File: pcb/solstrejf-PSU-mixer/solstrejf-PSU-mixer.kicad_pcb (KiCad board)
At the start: 2 copper layers, 36 parts, among them J1 LEFT_JACK, J2 RIGHT_JACK, J3 Conn_02x05_Odd_Even, J4 Conn_02x05_Odd_Even, J5 Conn_02x05_Odd_Even, J6 Conn_02x05_Odd_Even, J7 Transformer_Terminals, U1 Opamp_Dual, U2 L7815, U3 L7915

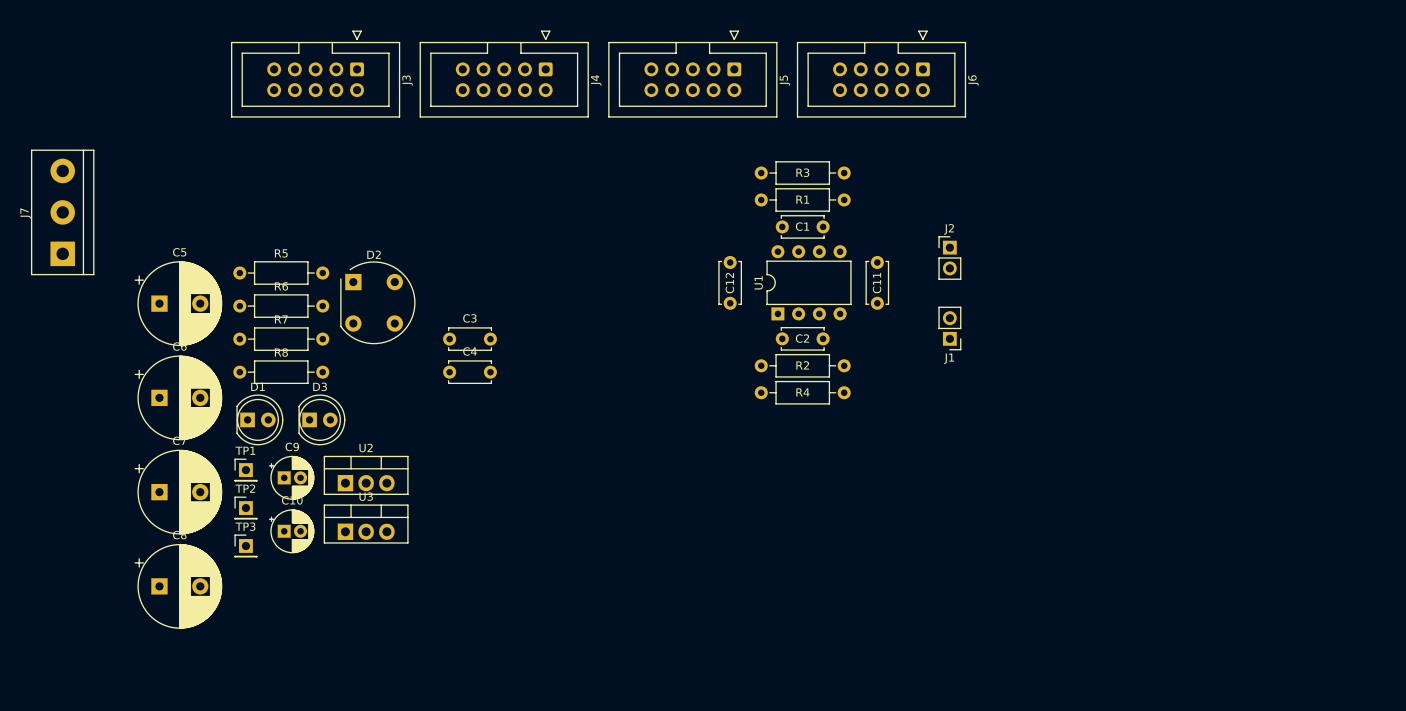
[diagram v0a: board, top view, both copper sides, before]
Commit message: updated KiCad schematic and PCB with the new changes added to the TIA after LTspice simulations.
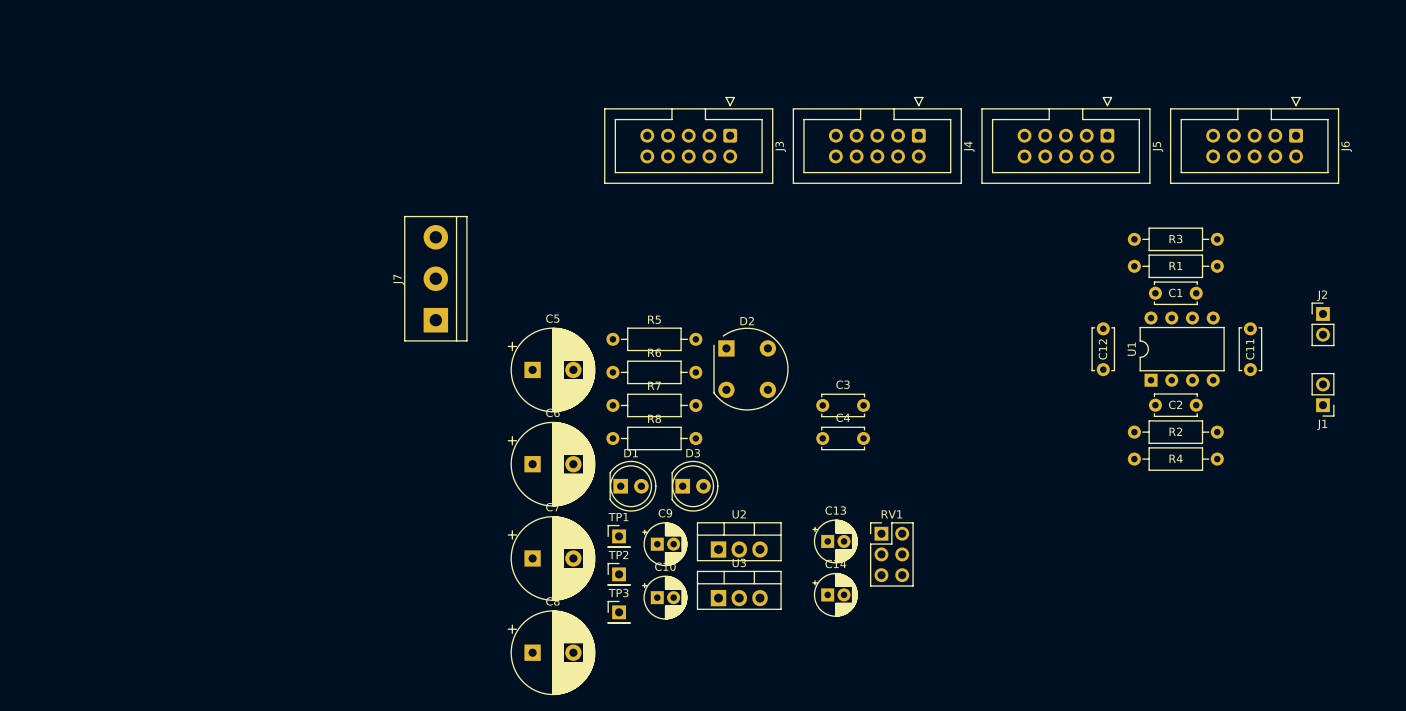
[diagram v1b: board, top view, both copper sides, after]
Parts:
- added C13: 1uF, Capacitor_THT:CP_Radial_D5.0mm_P2.00mm, F.Cu at (115.3, 114.5)
- added C14: 1uF, Capacitor_THT:CP_Radial_D5.0mm_P2.00mm, F.Cu at (115.3, 121.0)
- added RV1: 100k-A, Connector_PinHeader_2.54mm:PinHeader_2x03_P2.54mm_Vertical, F.Cu at (121.9, 113.5)
- C1, C2: value 2n2 -> 1nF
- R1, R2: value 5k -> 10k
- moved C12 46.4 mm to (149.1, 93.4)
- moved R1 46.4 mm to (163.1, 80.8)
- moved R2 46.4 mm to (163.1, 101.1)
- moved C10 46.4 mm to (94.5, 121.4)
- moved C5 46.4 mm to (79.2, 93.5)
- moved C6 46.4 mm to (79.2, 105.0)
- moved C7 46.4 mm to (79.2, 116.6)
- moved C8 46.4 mm to (79.2, 128.1)
- moved C9 46.4 mm to (94.5, 114.8)
- moved D2 46.4 mm to (102.9, 90.8)
- moved D3 46.4 mm to (97.6, 107.7)
- moved R5 46.4 mm to (89.0, 89.7)
- moved R6 46.4 mm to (89.0, 93.8)
- moved R7 46.4 mm to (89.0, 97.8)
- moved R8 46.4 mm to (89.0, 101.9)
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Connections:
- R3 pad 2: /R_OUT -> Net-(C14-Pad1)
- R4 pad 2: /L_OUT -> Net-(C13-Pad1)

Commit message: made first attempt of a PCB layout onf the PSU/mixer. No routing performed. Minor updates to schematic, including mounting holes.
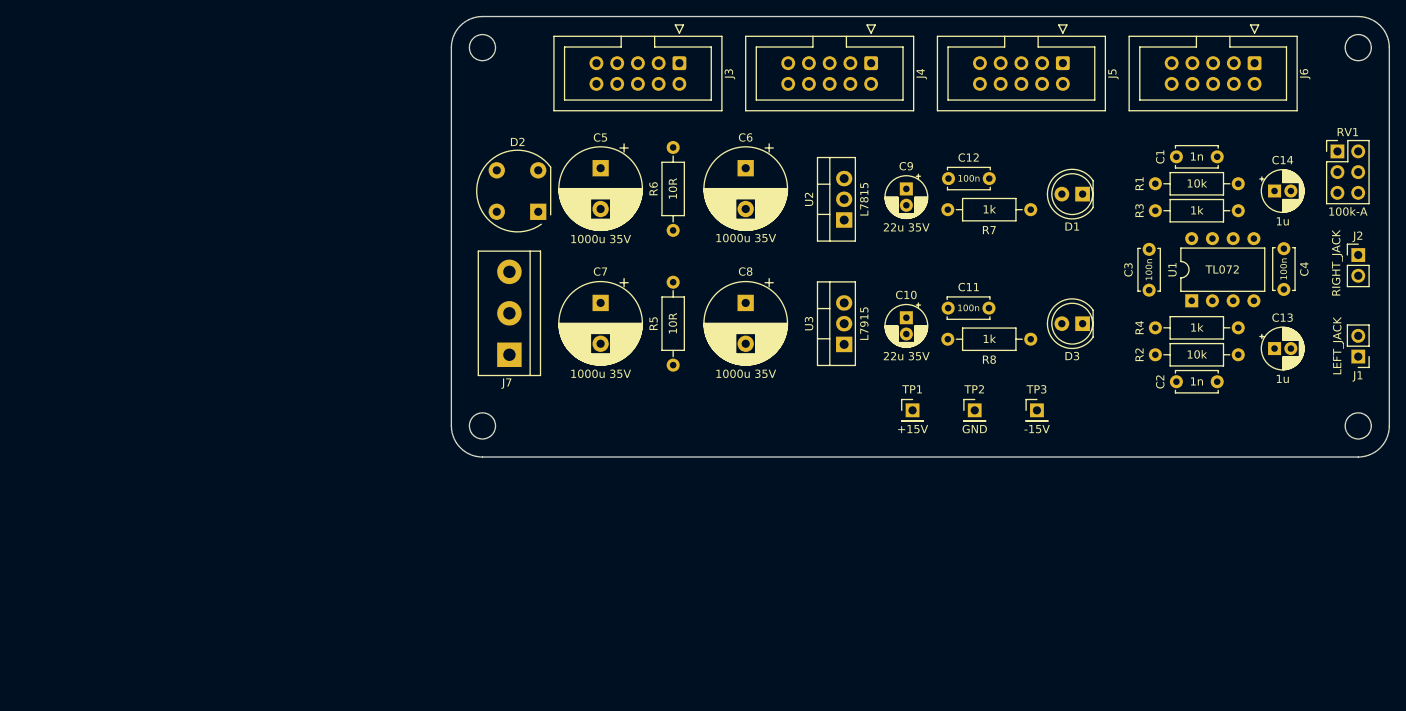
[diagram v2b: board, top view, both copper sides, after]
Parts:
- added H1: MountingHole, MountingHole:MountingHole_3.2mm_M3_DIN965, F.Cu at (73.0, 54.0)
- added H2: MountingHole, MountingHole:MountingHole_3.2mm_M3_DIN965, F.Cu at (180.3, 54.0)
- added H3: MountingHole, MountingHole:MountingHole_3.2mm_M3_DIN965, F.Cu at (180.3, 100.3)
- added H4: MountingHole, MountingHole:MountingHole_3.2mm_M3_DIN965, F.Cu at (73.0, 100.3)
- C1, C2: value 1nF -> 1n
- C10, C9: value 22uF 35V -> 22u 35V
- C13, C14: value 1uF -> 1u
- C5, C6, C7, C8: value 1000uF 35V -> 1000u 35V
- TP1: value +15V_TP -> +15V
- TP2: value GND_TP -> GND
- TP3: value -15V_TP -> -15V
- U1: value Opamp_Dual -> TL072
- moved C14 73.8 mm to (170.1, 71.5)
- moved RV1 72.9 mm to (177.8, 66.7)
- moved D1 67.0 mm to (146.6, 71.9), turned to 180 degrees
- moved C13 59.6 mm to (170.1, 90.9)
- moved C4 59.4 mm to (171.2, 83.6), turned to 90 degrees
- moved TP3 56.9 mm to (141.0, 98.4)
- moved R7 56.5 mm to (140.2, 73.8), turned to 180 degrees
- moved C9 53.2 mm to (125.0, 71.3), turned to -90 degrees
- moved D3 52.9 mm to (146.6, 87.8), turned to 180 degrees
- moved C8 50.2 mm to (105.3, 85.3), turned to -90 degrees
- moved TP2 48.0 mm to (133.3, 98.4)
- moved C10 45.9 mm to (125.0, 87.1), turned to -90 degrees
- moved C6 44.7 mm to (105.3, 68.8), turned to -90 degrees
- moved U2 43.2 mm to (117.3, 75.1), turned to 90 degrees
- moved R8 42.8 mm to (130.0, 89.7)
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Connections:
- C3 pad 1: Net-(C3-Pad1) -> GND
- C4 pad 2: Net-(C3-Pad1) -> GND
- D3 pad 1: -15V -> Net-(D3-K)
- D3 pad 2: Net-(D3-A) -> GND
- R8 pad 1: Net-(D3-A) -> -15V
- R8 pad 2: GND -> Net-(D3-K)
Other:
- board outline added: 114.9 x 54 mm

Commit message: routing of PSU/mixer done! Minor schematic updates. Added gerber production files to .gitignore.
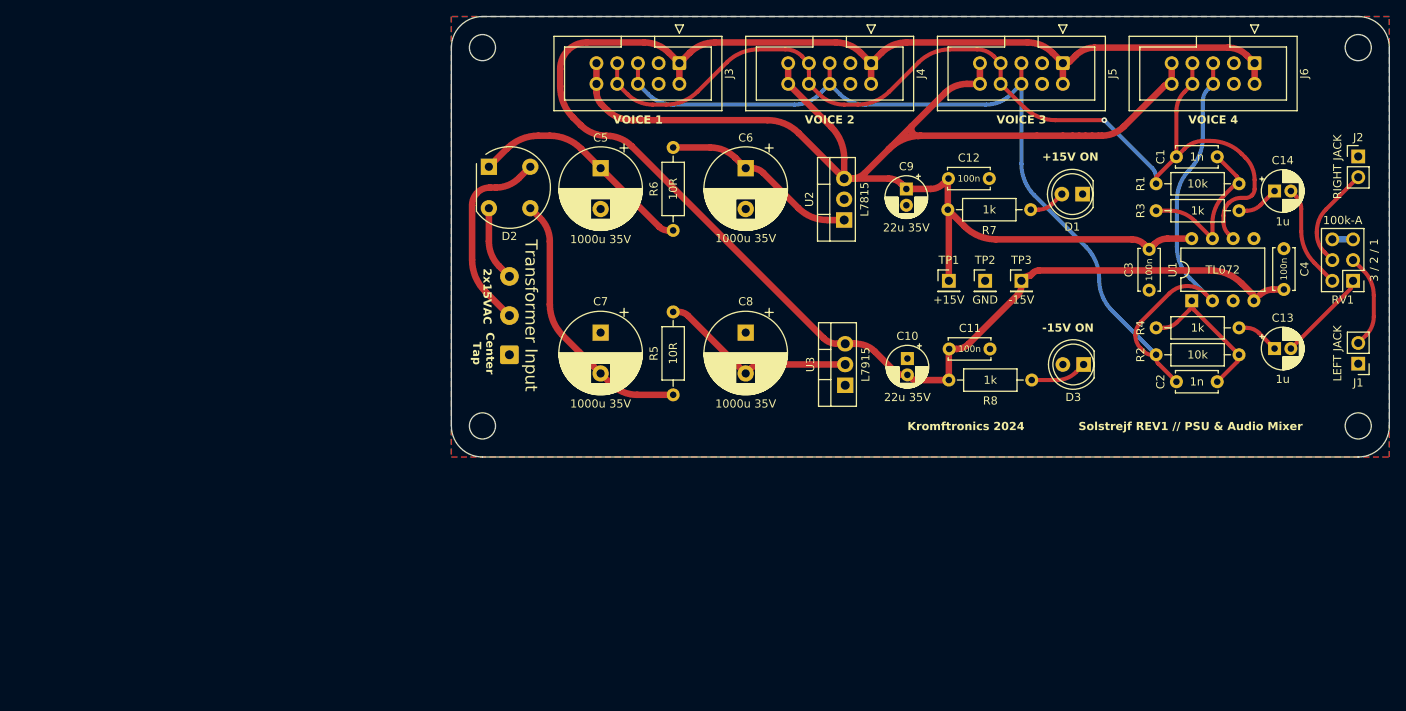
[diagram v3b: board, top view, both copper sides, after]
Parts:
- J1: value LEFT_JACK -> LEFT JACK
- J2: value RIGHT_JACK -> RIGHT JACK
- J7: footprint TerminalBlock:TerminalBlock_bornier-3_P5.08mm -> Connector_Wire:SolderWire-0.5sqmm_1x03_P4.8mm_D0.9mm_OD2.3mm
- moved TP1 16.5 mm to (130.2, 82.5)
- moved TP3 16.0 mm to (139.1, 82.5)
- moved RV1 16.0 mm to (179.7, 82.5), turned to 180 degrees
- moved TP2 15.9 mm to (134.6, 82.5)
- moved J2 12.1 mm to (180.3, 67.3)
- moved R3 10.1 mm to (155.6, 74.0), turned to 0 degrees
- moved R4 10.1 mm to (155.6, 88.3), turned to 0 degrees
- moved D2 8.19 mm to (73.8, 68.6), turned to 0 degrees
- moved C10 5.00 mm to (125.1, 92.1)
- moved C11 5.00 mm to (130.2, 90.9)
- moved D3 5.00 mm to (146.7, 92.8)
- moved U3 5.00 mm to (117.5, 95.3)
- moved R8 5.00 mm to (130.2, 94.7)
- moved C7 3.64 mm to (87.5, 88.9)
- moved C8 3.64 mm to (105.3, 88.9)
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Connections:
- J1 pad 1: /L_OUT -> GND
- J1 pad 2: GND -> /L_OUT
- J2 pad 1: /R_OUT -> GND
- J2 pad 2: GND -> /R_OUT
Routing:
- net -15V: track 0.00 -> 218.5 mm
- net +15V: track 0.00 -> 178.1 mm
- net /L_IN: track 0.00 -> 150.7 mm
- net /R_IN: track 0.00 -> 126.1 mm, vias 0 -> 1
- net Net-(D2--): track 0.00 -> 33.1 mm
- net Net-(D2-+): track 0.00 -> 28.4 mm
- net /AC_1: track 0.00 -> 24.4 mm
- net Net-(U3-VI): track 0.00 -> 24.3 mm
- net Net-(U2-IN): track 0.00 -> 24.1 mm
- net Net-(C1-Pad2): track 0.00 -> 20.5 mm
- net Net-(C2-Pad2): track 0.00 -> 19.3 mm
- net Net-(C14-Pad2): track 0.00 -> 12.7 mm
- net /R_OUT: track 0.00 -> 12.7 mm
- net /L_OUT: track 0.00 -> 11.6 mm
- net Net-(C13-Pad2): track 0.00 -> 11.4 mm
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- added copper zone on B.Cu, net GND
- added copper zone on F.Cu, net GND
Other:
- board text added: "+15V ON"
- board text added: "-15V ON"
- board text added: "2x15VAC"
- board text added: "3 / 2 / 1"
- board text added: "Center Tap"
- board text added: "Kromftronics 2024"
- board text added: "Solstrejf REV1 // PSU & Audio Mixer"
- board text added: "Transformer Input"
- board text added: "VOICE 1"
- board text added: "VOICE 2"
- board text added: "VOICE 3"
- board text added: "VOICE 4"

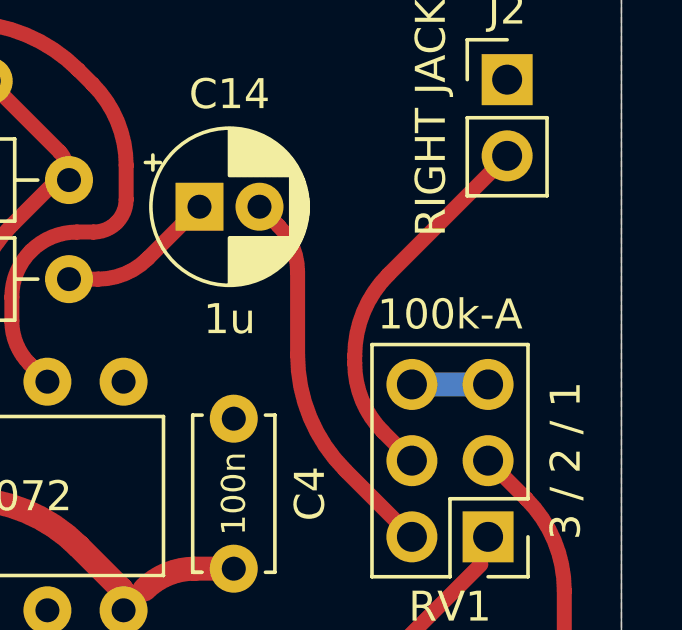
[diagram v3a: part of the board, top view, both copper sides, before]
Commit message: Updated LTspice simulation of output TIA with decrease volume pot for 15.92Hz highpass frequency. Updated KiCad and images with the same change.
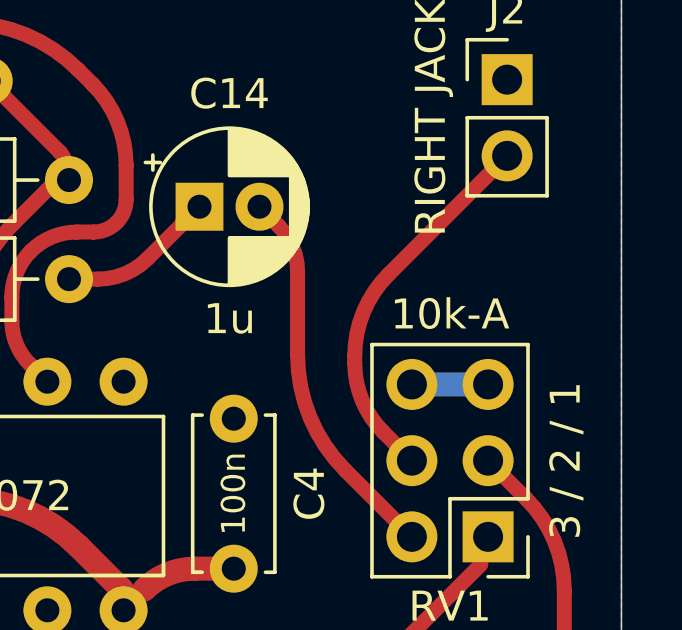
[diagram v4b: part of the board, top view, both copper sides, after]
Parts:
- RV1: value 100k-A -> 10k-A
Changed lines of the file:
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@@
 			)
 		)
-		(property "Value" "100k-A"
+		(property "Value" "10k-A"
 			(at 1.27 7.41 0)
 			(layer "F.SilkS")
@@
 		(tags "Through hole pin header THT 1x02 2.54mm single row")
 		(property "Reference" "J1"
-			(at 0 -2.33 360)
+			(at 0 -2.33 0)
 			(layer "F.SilkS")
 			(effects
@@
 		(tags "Through hole pin header THT 1x02 2.54mm single row")
 		(property "Reference" "J2"
-			(at 0 -2.33 360)
+			(at 0 -2.33 0)
 			(layer "F.SilkS")
 			(effects
